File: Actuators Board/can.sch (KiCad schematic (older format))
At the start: 3 parts

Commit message: Place Hierarchical Pins from CAN sheet to each board.
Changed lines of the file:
@@
 Wire Wire Line
 	1400 1850 1400 2150
-Text Label 1200 1650 0    50   ~ 0
-CAN_RX
-Text Label 1200 1550 0    50   ~ 0
-CAN_TX
 Wire Wire Line
 	1400 1650 1200 1650
@@
 Wire Wire Line
 	2200 1650 2500 1650
+Text HLabel 1200 1550 0    50   Input ~ 0
+CAN_TX
+Text HLabel 1200 1650 0    50   Output ~ 0
+CAN_RX
 $EndSCHEMATC

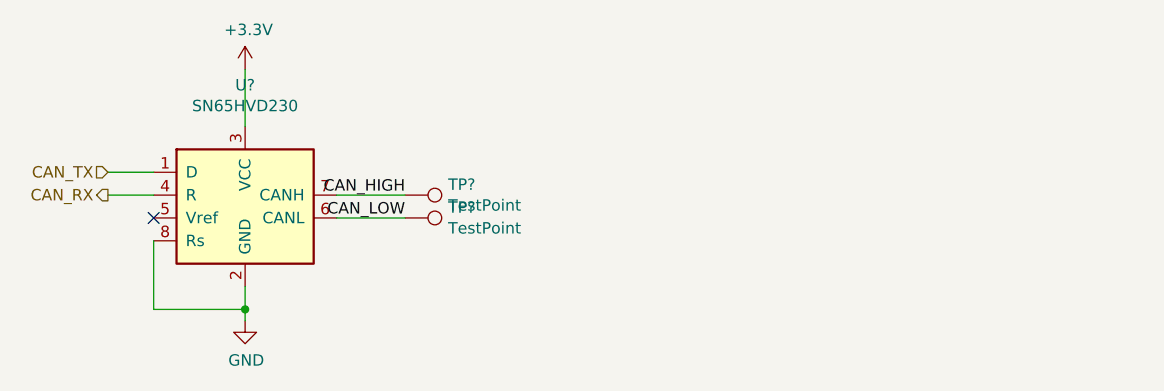
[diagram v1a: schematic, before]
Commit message: Added connector to CAN sheet
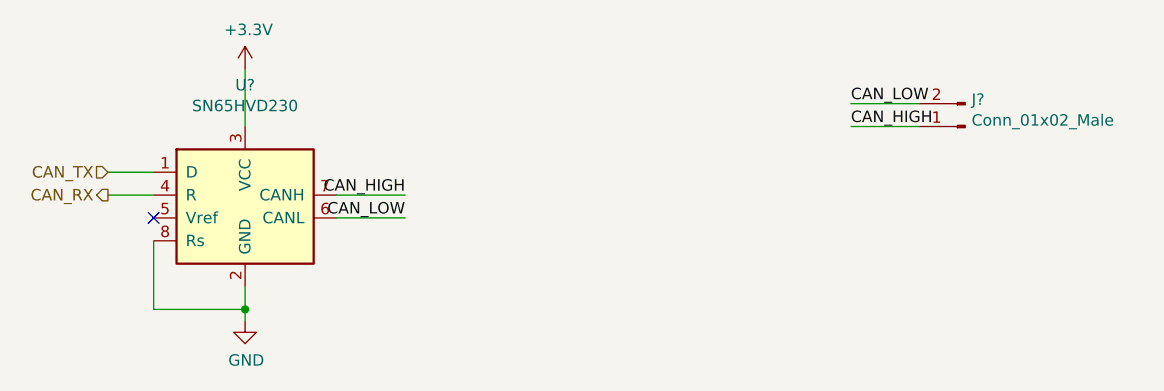
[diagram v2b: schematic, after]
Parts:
- removed TP? (x2): TestPoint, TestPoint:TestPoint_THTPad_1.0x1.0mm_Drill0.5mm, symbol Connector:TestPoint
- added J?: Conn_01x02_Male, symbol Connector:Conn_01x02_Male
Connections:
- net CAN_HIGH: now also J?.1 (Pin_1)
- net CAN_LOW: now also J?.2 (Pin_2)
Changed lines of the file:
@@
 $Descr A4 11693 8268
 encoding utf-8
-Sheet 3 4
+Sheet 1 1
 Title ""
 Date ""
@@
 $EndComp
 NoConn ~ 1400 1750
-$Comp
-L Connector:TestPoint TP?
-U 1 1 61946ECA
-P 2500 1650
-F 0 "TP?" V 2454 1838 50  0000 L CNN
-F 1 "TestPoint" V 2545 1838 50  0000 L CNN
-F 2 "TestPoint:TestPoint_THTPad_1.0x1.0mm_Drill0.5mm" H 2700 1650 50  0001 C CNN
-F 3 "~" H 2700 1650 50  0001 C CNN
-	1    2500 1650
-	0    1    1    0
-$EndComp
-$Comp
-L Connector:TestPoint TP?
-U 1 1 61946ED0
-P 2500 1750
-F 0 "TP?" V 2454 1938 50  0000 L CNN
-F 1 "TestPoint" V 2545 1938 50  0000 L CNN
-F 2 "TestPoint:TestPoint_THTPad_1.0x1.0mm_Drill0.5mm" H 2700 1750 50  0001 C CNN
-F 3 "~" H 2700 1750 50  0001 C CNN
-	1    2500 1750
-	0    1    1    0
-$EndComp
 Wire Wire Line
 	2200 1650 2500 1650
@@
 Text HLabel 1200 1650 0    50   Output ~ 0
 CAN_RX
+$Comp
+L Connector:Conn_01x02_Male J?
+U 1 1 61AFAFC6
+P 4950 1350
+F 0 "J?" H 4922 1232 50  0000 R CNN
+F 1 "Conn_01x02_Male" H 4922 1323 50  0000 R CNN
+F 2 "" H 4950 1350 50  0001 C CNN
+F 3 "~" H 4950 1350 50  0001 C CNN
+	1    4950 1350
+	-1   0    0    1
+$EndComp
+Text Label 4450 1250 0    50   ~ 0
+CAN_LOW
+Text Label 4450 1350 0    50   ~ 0
+CAN_HIGH
+Wire Wire Line
+	4750 1250 4450 1250
+Wire Wire Line
+	4750 1350 4450 1350
 $EndSCHEMATC

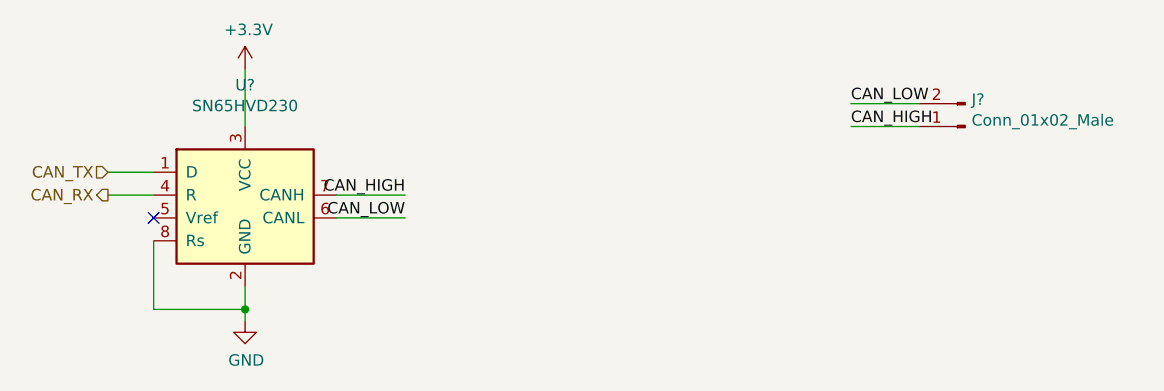
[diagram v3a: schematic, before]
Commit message: Changed main connector to 5 pins, added cool LEDs (needlevalveboard)
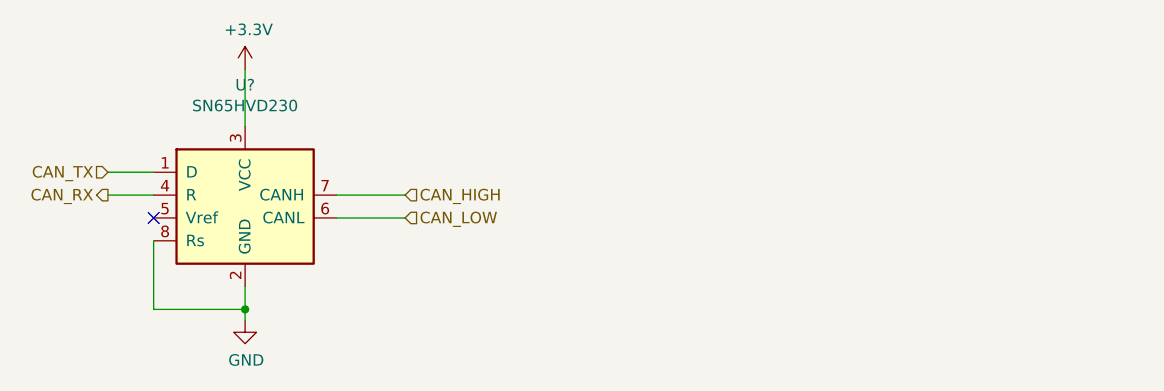
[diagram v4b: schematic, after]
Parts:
- removed J?: Conn_01x02_Male, symbol Connector:Conn_01x02_Male
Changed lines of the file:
@@
 $Descr A4 11693 8268
 encoding utf-8
-Sheet 1 4
+Sheet 3 4
 Title ""
 Date ""
@@
 	1    0    0    -1
 $EndComp
-Text Label 2500 1750 2    50   ~ 0
-CAN_LOW
-Text Label 2500 1650 2    50   ~ 0
-CAN_HIGH
 Wire Wire Line
 	2200 1750 2500 1750
@@
 Text HLabel 1200 1650 0    50   Output ~ 0
 CAN_RX
-$Comp
-L Connector:Conn_01x02_Male J?
-U 1 1 61AFAFC6
-P 4950 1350
-F 0 "J?" H 4922 1232 50  0000 R CNN
-F 1 "Conn_01x02_Male" H 4922 1323 50  0000 R CNN
-F 2 "" H 4950 1350 50  0001 C CNN
-F 3 "~" H 4950 1350 50  0001 C CNN
-	1    4950 1350
-	-1   0    0    1
-$EndComp
-Text Label 4450 1250 0    50   ~ 0
+Text HLabel 2500 1650 2    50   Input ~ 0
+CAN_HIGH
+Text HLabel 2500 1750 2    50   Input ~ 0
 CAN_LOW
-Text Label 4450 1350 0    50   ~ 0
-CAN_HIGH
-Wire Wire Line
-	4750 1250 4450 1250
-Wire Wire Line
-	4750 1350 4450 1350
 $EndSCHEMATC

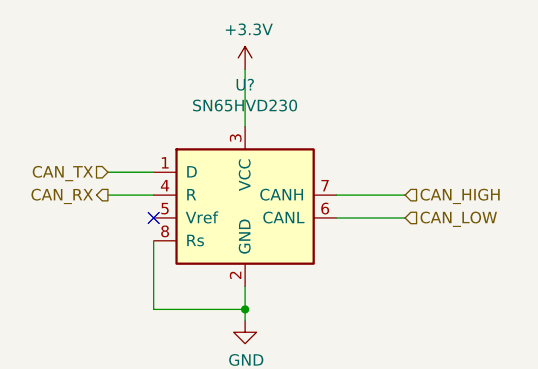
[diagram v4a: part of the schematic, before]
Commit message: Most footprint assignments on dc motor board
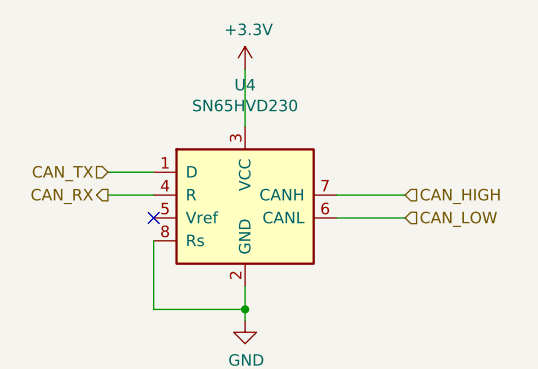
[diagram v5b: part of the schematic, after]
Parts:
- gave numbers to parts that had none: 1
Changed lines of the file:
@@
 	1800 2200 1800 2150
 $Comp
-L power:GND #PWR?
+L power:GND #PWR0130
 U 1 1 61946EB3
 P 1800 2200
-F 0 "#PWR?" H 1800 1950 50  0001 C CNN
+F 0 "#PWR0130" H 1800 1950 50  0001 C CNN
 F 1 "GND" H 1805 2027 50  0000 C CNN
 F 2 "" H 1800 2200 50  0001 C CNN
@@
 $EndComp
 $Comp
-L power:+3.3V #PWR?
+L power:+3.3V #PWR0131
 U 1 1 61946EB9
 P 1800 1100
-F 0 "#PWR?" H 1800 950 50  0001 C CNN
+F 0 "#PWR0131" H 1800 950 50  0001 C CNN
 F 1 "+3.3V" H 1815 1273 50  0000 C CNN
 F 2 "" H 1800 1100 50  0001 C CNN
@@
 	1800 1100 1800 1350
 $Comp
-L Interface_CAN_LIN:SN65HVD230 U?
+L Interface_CAN_LIN:SN65HVD230 U4
 U 1 1 61946EC3
 P 1800 1650
-F 0 "U?" H 1800 2131 50  0000 C CNN
+F 0 "U4" H 1800 2131 50  0000 C CNN
 F 1 "SN65HVD230" H 1800 2040 50  0000 C CNN
 F 2 "Package_SO:SOIC-8_3.9x4.9mm_P1.27mm" H 1800 1150 50  0001 C CNN
